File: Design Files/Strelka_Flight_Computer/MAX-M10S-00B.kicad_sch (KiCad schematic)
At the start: 16 parts

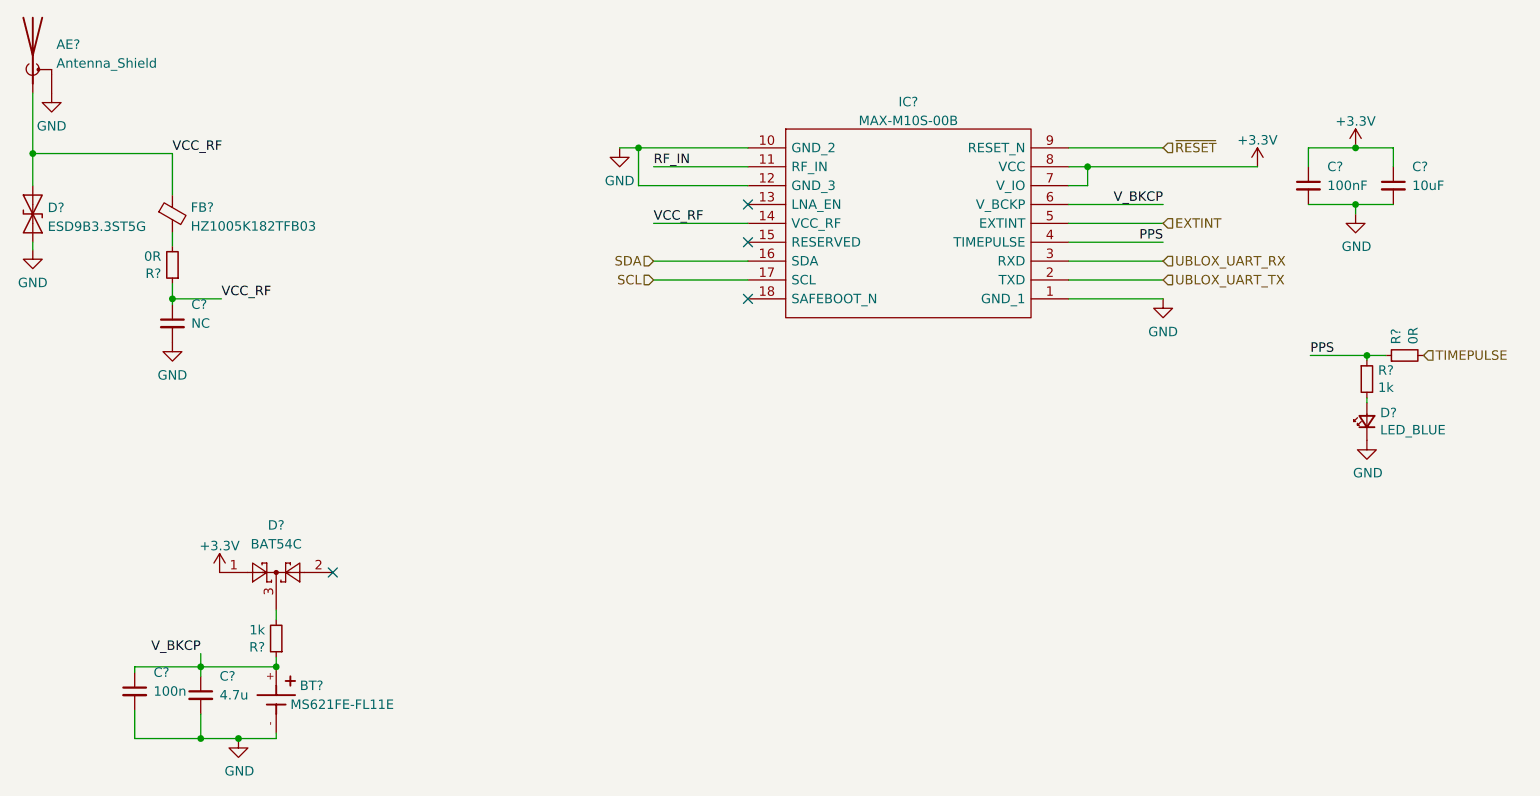
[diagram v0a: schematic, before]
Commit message: Added motor driver to power board
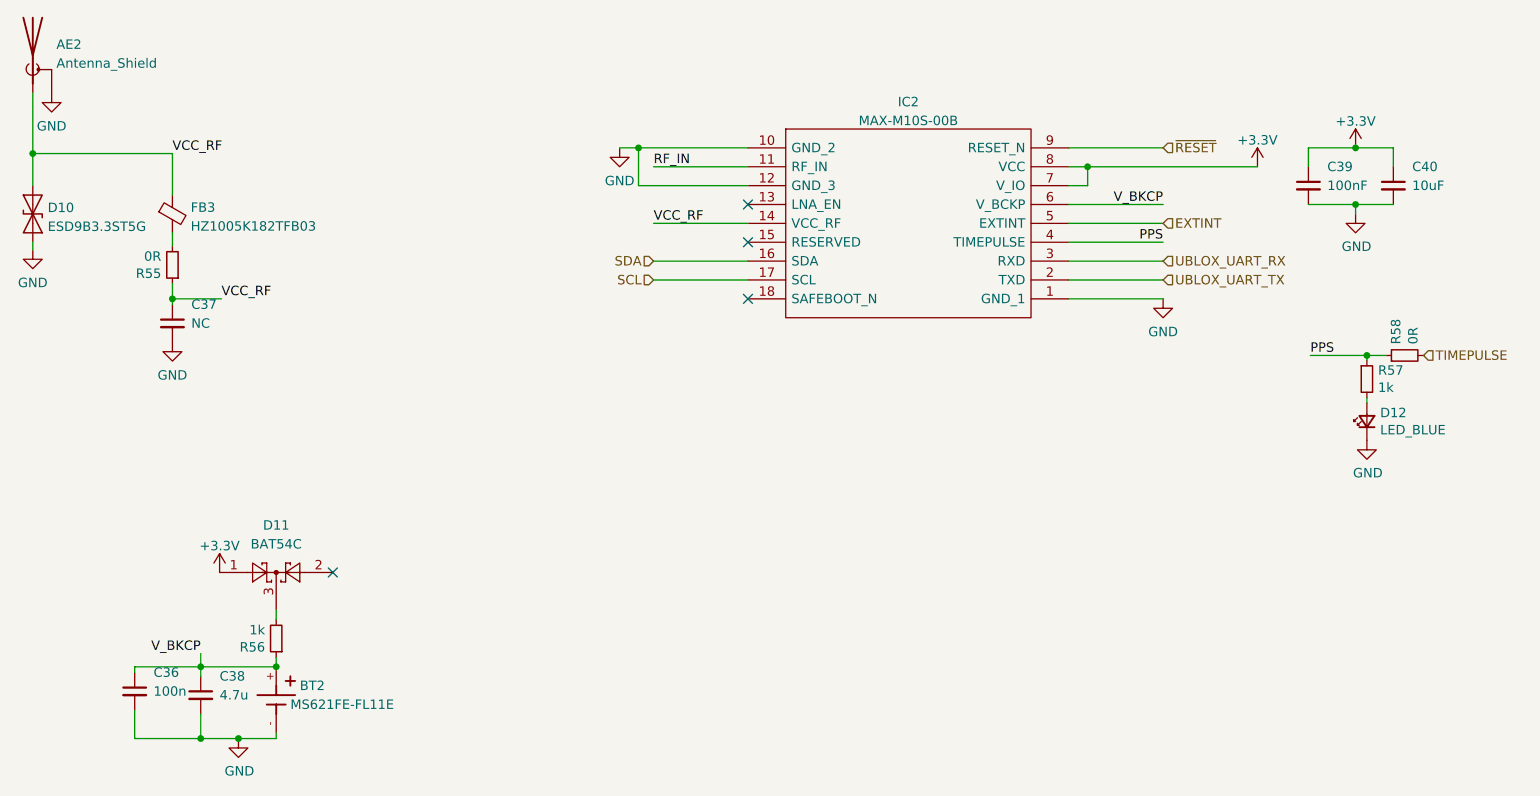
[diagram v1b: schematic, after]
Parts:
- gave numbers to parts that had none: 16
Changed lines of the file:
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@@
   (symbol (lib_id "power:GND") (at 187.452 104.14 0) (unit 1)
     (in_bom yes) (on_board yes) (fields_autoplaced)
-    (property "Reference" "#PWR?" (id 0) (at 187.452 110.49 0)
+    (property "Reference" "#PWR0208" (id 0) (at 187.452 110.49 0)
       (effects (font (size 1.27 1.27)) hide)
     )
@@
   (symbol (lib_id "MS621FE-FL11E:MS621FE-FL11E") (at 68.072 158.115 270) (unit 1)
     (in_bom yes) (on_board yes)
-    (property "Reference" "BT?" (id 0) (at 71.247 156.21 90)
+    (property "Reference" "BT2" (id 0) (at 71.247 156.21 90)
       (effects (font (size 1.27 1.27)) (justify left))
     )
@@
   (symbol (lib_id "Device:R_Small") (at 219.964 111.76 90) (unit 1)
     (in_bom yes) (on_board yes)
-    (property "Reference" "R?" (id 0) (at 218.7956 110.2614 0)
+    (property "Reference" "R58" (id 0) (at 218.7956 110.2614 0)
       (effects (font (size 1.27 1.27)) (justify left))
     )
@@
   (symbol (lib_id "power:GND") (at 214.884 123.19 0) (unit 1)
     (in_bom yes) (on_board yes)
-    (property "Reference" "#PWR?" (id 0) (at 214.884 129.54 0)
+    (property "Reference" "#PWR0211" (id 0) (at 214.884 129.54 0)
       (effects (font (size 1.27 1.27)) hide)
     )
@@
   (symbol (lib_id "power:GND") (at 114.3 83.82 0) (unit 1)
     (in_bom yes) (on_board yes) (fields_autoplaced)
-    (property "Reference" "#PWR?" (id 0) (at 114.3 90.17 0)
+    (property "Reference" "#PWR0205" (id 0) (at 114.3 90.17 0)
       (effects (font (size 1.27 1.27)) hide)
     )
@@
   (symbol (lib_id "power:GND") (at 213.36 92.71 0) (unit 1)
     (in_bom yes) (on_board yes)
-    (property "Reference" "#PWR?" (id 0) (at 213.36 99.06 0)
+    (property "Reference" "#PWR0207" (id 0) (at 213.36 99.06 0)
       (effects (font (size 1.27 1.27)) hide)
     )
@@
   (symbol (lib_id "MAX-M10S-00B:MAX-M10S-00B") (at 131.572 83.82 0) (unit 1)
     (in_bom yes) (on_board yes) (fields_autoplaced)
-    (property "Reference" "IC?" (id 0) (at 153.162 77.631 0))
+    (property "Reference" "IC2" (id 0) (at 153.162 77.631 0))
     (property "Value" "MAX-M10S-00B" (id 1) (at 153.162 80.1679 0))
     (property "Footprint" "Footprints:MAXM10S00B" (id 2) (at 170.942 81.28 0)
@@
   (symbol (lib_id "Device:C_Small") (at 218.44 88.9 0) (unit 1)
     (in_bom yes) (on_board yes)
-    (property "Reference" "C?" (id 0) (at 220.98 86.36 0)
+    (property "Reference" "C40" (id 0) (at 220.98 86.36 0)
       (effects (font (size 1.27 1.27)) (justify left))
     )
@@
   (symbol (lib_id "Device:C_Small") (at 207.01 88.9 0) (unit 1)
     (in_bom yes) (on_board yes)
-    (property "Reference" "C?" (id 0) (at 209.55 86.36 0)
+    (property "Reference" "C39" (id 0) (at 209.55 86.36 0)
       (effects (font (size 1.27 1.27)) (justify left))
     )
@@
   (symbol (lib_id "Device:FerriteBead_Small") (at 54.102 92.71 0) (unit 1)
     (in_bom yes) (on_board yes) (fields_autoplaced)
-    (property "Reference" "FB?" (id 0) (at 56.5658 91.8372 0)
+    (property "Reference" "FB3" (id 0) (at 56.5658 91.8372 0)
       (effects (font (size 1.27 1.27)) (justify left))
     )
@@
   (symbol (lib_id "power:GND") (at 62.992 163.322 0) (unit 1)
     (in_bom yes) (on_board yes)
-    (property "Reference" "#PWR?" (id 0) (at 62.992 169.672 0)
+    (property "Reference" "#PWR0213" (id 0) (at 62.992 169.672 0)
       (effects (font (size 1.27 1.27)) hide)
     )
@@
   (symbol (lib_id "power:+3.3V") (at 200.152 86.36 0) (unit 1)
     (in_bom yes) (on_board yes) (fields_autoplaced)
-    (property "Reference" "#PWR?" (id 0) (at 200.152 90.17 0)
+    (property "Reference" "#PWR0210" (id 0) (at 200.152 90.17 0)
       (effects (font (size 1.27 1.27)) hide)
     )
@@
   (symbol (lib_id "Device:C_Small") (at 57.912 157.48 0) (unit 1)
     (in_bom yes) (on_board yes)
-    (property "Reference" "C?" (id 0) (at 60.452 154.94 0)
+    (property "Reference" "C38" (id 0) (at 60.452 154.94 0)
       (effects (font (size 1.27 1.27)) (justify left))
     )
@@
   (symbol (lib_id "power:+3.3V") (at 213.36 83.82 0) (unit 1)
     (in_bom yes) (on_board yes) (fields_autoplaced)
-    (property "Reference" "#PWR?" (id 0) (at 213.36 87.63 0)
+    (property "Reference" "#PWR0209" (id 0) (at 213.36 87.63 0)
       (effects (font (size 1.27 1.27)) hide)
     )
@@
   (symbol (lib_id "power:GND") (at 35.306 97.536 0) (unit 1)
     (in_bom yes) (on_board yes) (fields_autoplaced)
-    (property "Reference" "#PWR?" (id 0) (at 35.306 103.886 0)
+    (property "Reference" "#PWR0206" (id 0) (at 35.306 103.886 0)
       (effects (font (size 1.27 1.27)) hide)
     )
@@
   (symbol (lib_id "power:+3.3V") (at 60.452 140.97 0) (unit 1)
     (in_bom yes) (on_board yes) (fields_autoplaced)
-    (property "Reference" "#PWR?" (id 0) (at 60.452 144.78 0)
+    (property "Reference" "#PWR0214" (id 0) (at 60.452 144.78 0)
       (effects (font (size 1.27 1.27)) hide)
     )
@@
   (symbol (lib_id "Diode:ESD9B3.3ST5G") (at 35.306 92.71 90) (unit 1)
     (in_bom yes) (on_board yes) (fields_autoplaced)
-    (property "Reference" "D?" (id 0) (at 37.3126 91.8753 90)
+    (property "Reference" "D10" (id 0) (at 37.3126 91.8753 90)
       (effects (font (size 1.27 1.27)) (justify right))
     )
@@
   (symbol (lib_id "Device:R_Small") (at 54.102 99.568 180) (unit 1)
     (in_bom yes) (on_board yes)
-    (property "Reference" "R?" (id 0) (at 52.6034 100.7364 0)
+    (property "Reference" "R55" (id 0) (at 52.6034 100.7364 0)
       (effects (font (size 1.27 1.27)) (justify left))
     )
@@
   (symbol (lib_id "Device:C_Small") (at 49.022 156.972 0) (unit 1)
     (in_bom yes) (on_board yes)
-    (property "Reference" "C?" (id 0) (at 51.562 154.432 0)
+    (property "Reference" "C36" (id 0) (at 51.562 154.432 0)
       (effects (font (size 1.27 1.27)) (justify left))
     )
@@
   (symbol (lib_id "Device:Antenna_Shield") (at 35.306 71.374 0) (unit 1)
     (in_bom yes) (on_board yes) (fields_autoplaced)
-    (property "Reference" "AE?" (id 0) (at 38.481 69.9043 0)
+    (property "Reference" "AE2" (id 0) (at 38.481 69.9043 0)
       (effects (font (size 1.27 1.27)) (justify left))
     )
@@
   (symbol (lib_id "Device:LED_Small") (at 214.884 120.65 90) (unit 1)
     (in_bom yes) (on_board yes)
-    (property "Reference" "D?" (id 0) (at 216.662 119.4816 90)
+    (property "Reference" "D12" (id 0) (at 216.662 119.4816 90)
       (effects (font (size 1.27 1.27)) (justify right))
     )
@@
   (symbol (lib_id "Device:R_Small") (at 68.072 149.86 180) (unit 1)
     (in_bom yes) (on_board yes)
-    (property "Reference" "R?" (id 0) (at 66.5734 151.0284 0)
+    (property "Reference" "R56" (id 0) (at 66.5734 151.0284 0)
       (effects (font (size 1.27 1.27)) (justify left))
     )
@@
   (symbol (lib_id "power:GND") (at 54.102 109.982 0) (unit 1)
     (in_bom yes) (on_board yes) (fields_autoplaced)
-    (property "Reference" "#PWR?" (id 0) (at 54.102 116.332 0)
+    (property "Reference" "#PWR0212" (id 0) (at 54.102 116.332 0)
       (effects (font (size 1.27 1.27)) hide)
     )
@@
   (symbol (lib_id "Device:C_Small") (at 54.102 107.442 0) (unit 1)
     (in_bom yes) (on_board yes)
-    (property "Reference" "C?" (id 0) (at 56.642 104.902 0)
+    (property "Reference" "C37" (id 0) (at 56.642 104.902 0)
       (effects (font (size 1.27 1.27)) (justify left))
     )
@@
   (symbol (lib_id "Device:R_Small") (at 214.884 114.935 0) (unit 1)
     (in_bom yes) (on_board yes)
-    (property "Reference" "R?" (id 0) (at 216.3826 113.7666 0)
+    (property "Reference" "R57" (id 0) (at 216.3826 113.7666 0)
       (effects (font (size 1.27 1.27)) (justify left))
     )
@@
   (symbol (lib_id "power:GND") (at 37.846 76.454 0) (unit 1)
     (in_bom yes) (on_board yes) (fields_autoplaced)
-    (property "Reference" "#PWR?" (id 0) (at 37.846 82.804 0)
+    (property "Reference" "#PWR0204" (id 0) (at 37.846 82.804 0)
       (effects (font (size 1.27 1.27)) hide)
     )
@@
   (symbol (lib_id "Diode:BAT54C") (at 68.072 140.97 0) (unit 1)
     (in_bom yes) (on_board yes) (fields_autoplaced)
-    (property "Reference" "D?" (id 0) (at 68.072 134.62 0))
+    (property "Reference" "D11" (id 0) (at 68.072 134.62 0))
     (property "Value" "BAT54C" (id 1) (at 68.072 137.16 0))
     (property "Footprint" "Package_TO_SOT_SMD:SOT-23" (id 2) (at 69.977 137.795 0)

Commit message: Changed boost converter
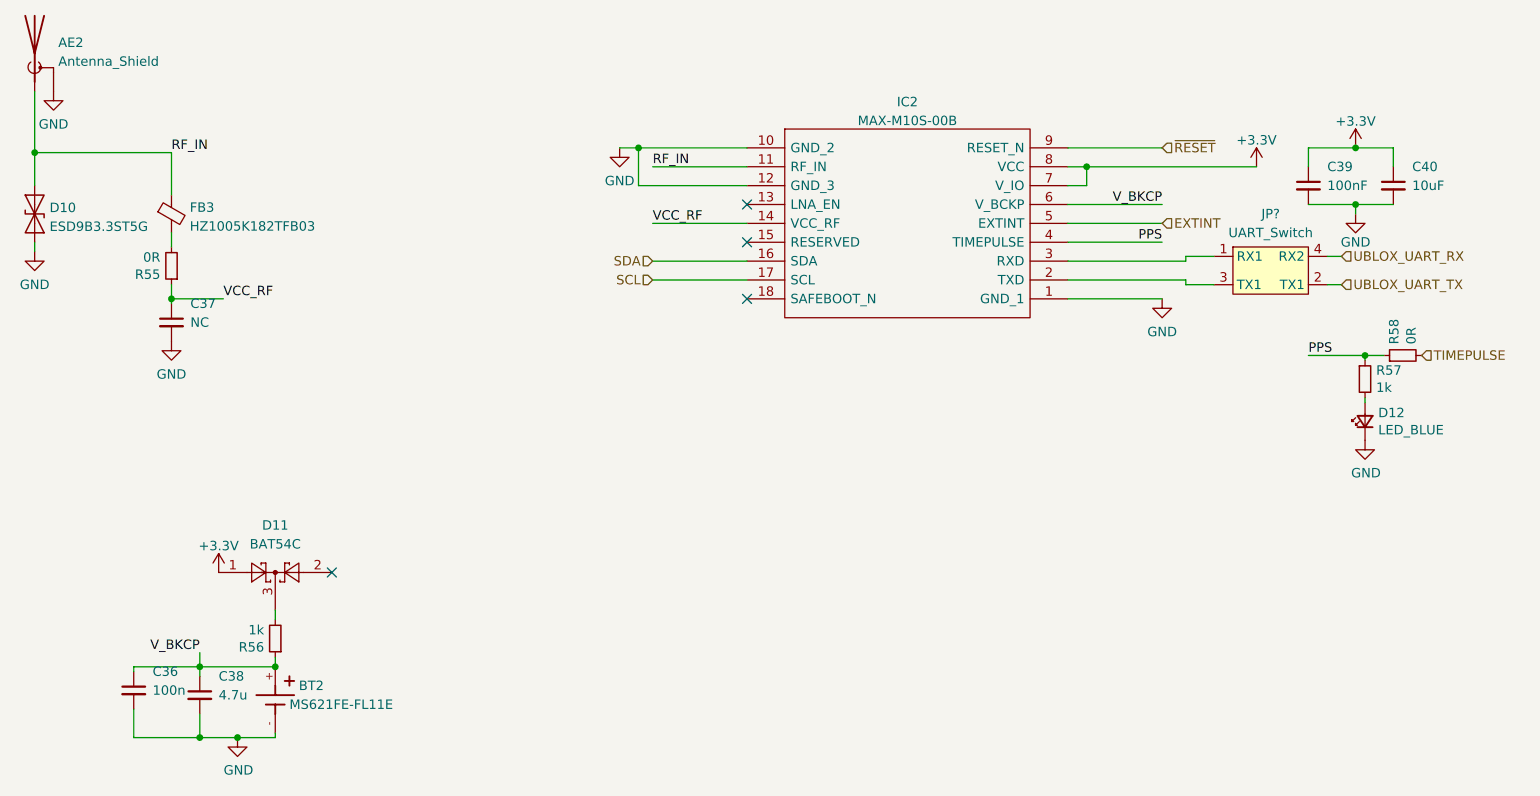
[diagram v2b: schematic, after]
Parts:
- added JP?: UART_Switch, Footprints:UART_Switch, symbol UART_Switch:UART_Switch
- BT2: footprint BAT_MS621FE-FL11E -> Footprints:BAT_MS621FE-FL11E
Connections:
- net RF_IN: now also AE2.1 (A), D10.2 (A2), FB3.1
- net UBLOX_UART_RX: now also JP?.4 (RX2); no longer IC2.3 (RXD)
- net UBLOX_UART_TX: now also JP?.2 (TX1); no longer IC2.2 (TXD)
- net VCC_RF: no longer AE2.1 (A), D10.2 (A2), FB3.1
- new net: IC2.2 (TXD), JP?.3 (TX1)
- new net: IC2.3 (RXD), JP?.1 (RX1)

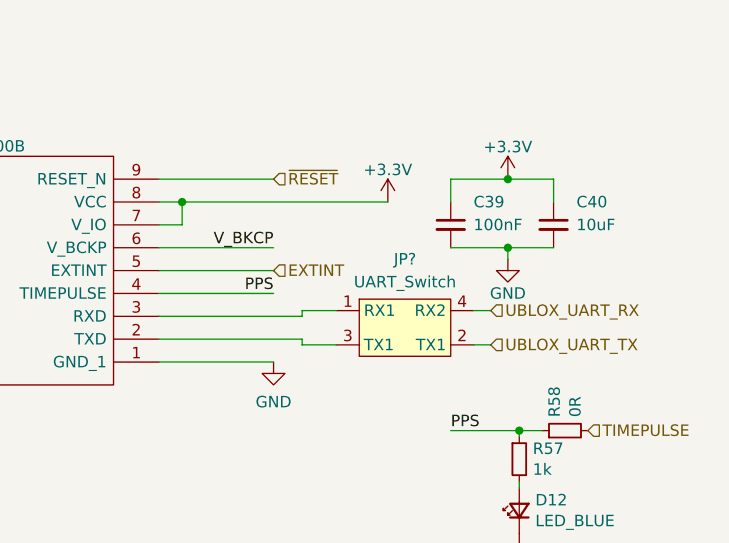
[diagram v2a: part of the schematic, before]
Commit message: Started component placement
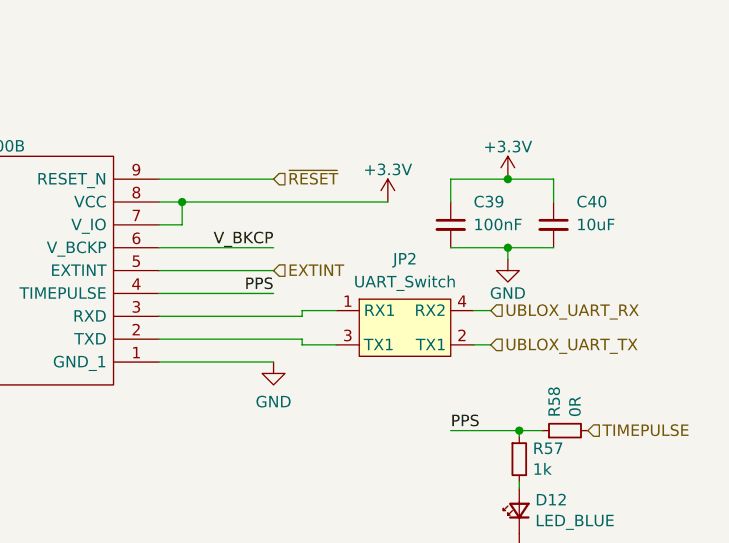
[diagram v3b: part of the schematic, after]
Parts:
- gave numbers to parts that had none: 1
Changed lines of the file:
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@@
   (symbol (lib_id "UART_Switch:UART_Switch") (at 201.93 100.965 0) (unit 1)
     (in_bom yes) (on_board yes)
-    (property "Reference" "JP?" (id 0) (at 201.93 92.71 0))
+    (property "Reference" "JP2" (id 0) (at 201.93 92.71 0))
     (property "Value" "UART_Switch" (id 1) (at 201.93 95.25 0))
     (property "Footprint" "Footprints:UART_Switch" (id 2) (at 201.93 100.965 0)

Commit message: Creating BOM
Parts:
- D11: LCSC# (none) -> C37704
- IC2: Height 2.7 -> (none); Link (none) -> https://www.digikey.com.au/en/products/detail/u-blox/MAX-M1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; Manufacturer_Name U-Blox -> (none); Manufacturer_Part_Number MAX-M10S-00B -> (none); Mouser Part Number 377-MAX-M10S-00B -> (none); Mouser Price/Stock https://www.mouser.co.uk/ProductDetail/u-blox/MAX-M10S-00B?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 -> (none)
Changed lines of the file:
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@@
       (effects (font (size 1.27 1.27)) (justify left) hide)
     )
-    (property "Description" "GPS Modules u-blox M10 GNSS LCC module, firmware in ROM, SAW filter, LNA" (id 4) (at 170.815 86.36 0)
-      (effects (font (size 1.27 1.27)) (justify left) hide)
-    )
-    (property "Height" "2.7" (id 5) (at 170.815 88.9 0)
-      (effects (font (size 1.27 1.27)) (justify left) hide)
-    )
-    (property "Manufacturer_Name" "U-Blox" (id 6) (at 170.815 91.44 0)
-      (effects (font (size 1.27 1.27)) (justify left) hide)
-    )
-    (property "Manufacturer_Part_Number" "MAX-M10S-00B" (id 7) (at 170.815 93.98 0)
-      (effects (font (size 1.27 1.27)) (justify left) hide)
-    )
-    (property "Mouser Part Number" "377-MAX-M10S-00B" (id 8) (at 170.815 96.52 0)
-      (effects (font (size 1.27 1.27)) (justify left) hide)
-    )
-    (property "Mouser Price/Stock" "https://www.mouser.co.uk/ProductDetail/u-blox/MAX-M10S-00B?qs=A6eO%252BMLsxmT0PfQYPb7LLQ%3D%3D" (id 9) (at 170.815 99.06 0)
-      (effects (font (size 1.27 1.27)) (justify left) hide)
-    )
-    (property "Arrow Part Number" "" (id 10) (at 170.815 101.6 0)
-      (effects (font (size 1.27 1.27)) (justify left) hide)
-    )
-    (property "Arrow Price/Stock" "" (id 11) (at 170.815 104.14 0)
-      (effects (font (size 1.27 1.27)) (justify left) hide)
-    )
-    (property "Mouser Testing Part Number" "" (id 12) (at 170.815 106.68 0)
-      (effects (font (size 1.27 1.27)) (justify left) hide)
-    )
-    (property "Mouser Testing Price/Stock" "" (id 13) (at 170.815 109.22 0)
+    (property "Link" "https://www.digikey.com.au/en/products/detail/u-blox/MAX-M10S-00B/15712906" (id 4) (at 170.815 86.36 0)
       (effects (font (size 1.27 1.27)) (justify left) hide)
     )
@@
       (effects (font (size 1.27 1.27)) hide)
     )
+    (property "LCSC#" "C37704" (id 4) (at 67.945 140.97 0)
+      (effects (font (size 1.27 1.27)) hide)
+    )
